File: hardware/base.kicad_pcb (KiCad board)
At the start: 4 copper layers, 100 x 85 mm, 316 parts, among them J101 USB-A, J102 TNG-Data-TOP, J103 TNG-Power-TOP, J301 MICROSDCARD, J302 Raspberry-Pi-Compute-Socket, J303 MICRO_HDMI, J304 USB Micro, J401 RJSLG-001TA1, P101 Debug, P102 Boot, P103 PE, P104 TST_GND, P105 TST_3V3P, P201 DI IN, P202 PWR IN, P203 TST_5V, P204 TST_GND, P301 TST_XMC_10, P302 TST_SCL, P303 TST_SDA, P304 TST_WP, P305 TST_3V3, P306 TST_1V8, P307 TST_XMC_11, P401 TST_1V2, Q301 2N7002P, Q302 2N7002P, Q303 2N7002P, Q304 2N7002P, Q305 2N7002P, T201 744272251, U101 USB2517, U102 MIC2026-1YM, U103 82400152, U104 XMC1302, U105 TPD4S010DQA, U106 TPD4S010DQA, U107 TPD4S010DQA, U108 AP7333-33SAG-7, U109 TPS22975, U110 TPS22975, U111 PCT2075DP, U112 VN7140AS, U201 ISO1211, U202 FPF2700MX, U203 BD90640HFP, U204 PAC1933, U301 PAM2306AYPAA, U302 PCF8523T, U303 FSUSB42MUX, U304 TPD4S010DQA, U305 TPD4S010DQA, U306 TPD4S010DQA, U307 82400152, U308 M24256-DFMN6TP, U309 AP2331, U310 SLB9670, U401 LAN7500, U402 93AA66, U403 TPD4S010DQA, U404 TPD4S010DQA, U405 PAM2306AYPAA, X101 24MHz, X301 32.768kHz, X401 25MHz_18pF

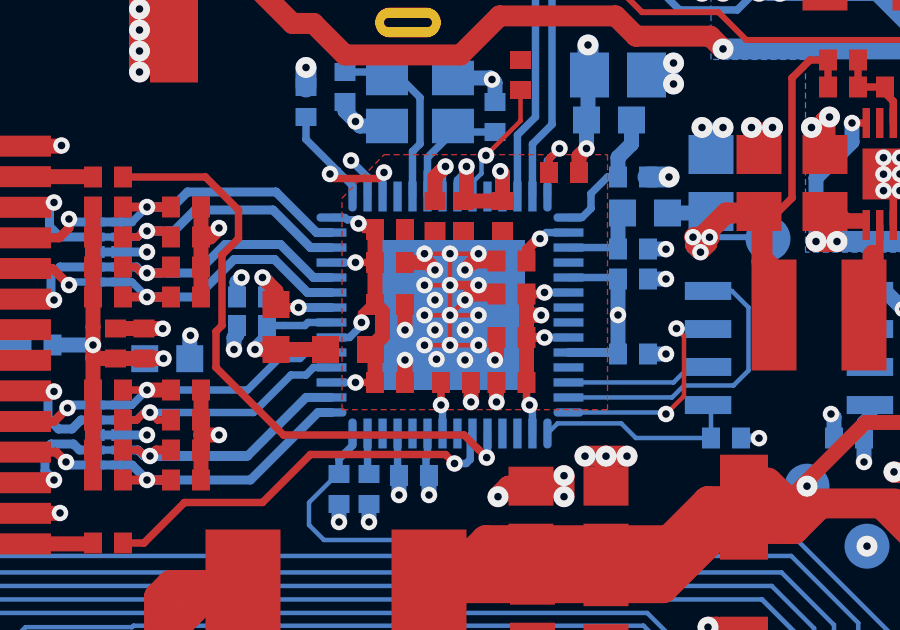
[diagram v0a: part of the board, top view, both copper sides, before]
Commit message: change ethernet capacitors to 33pF
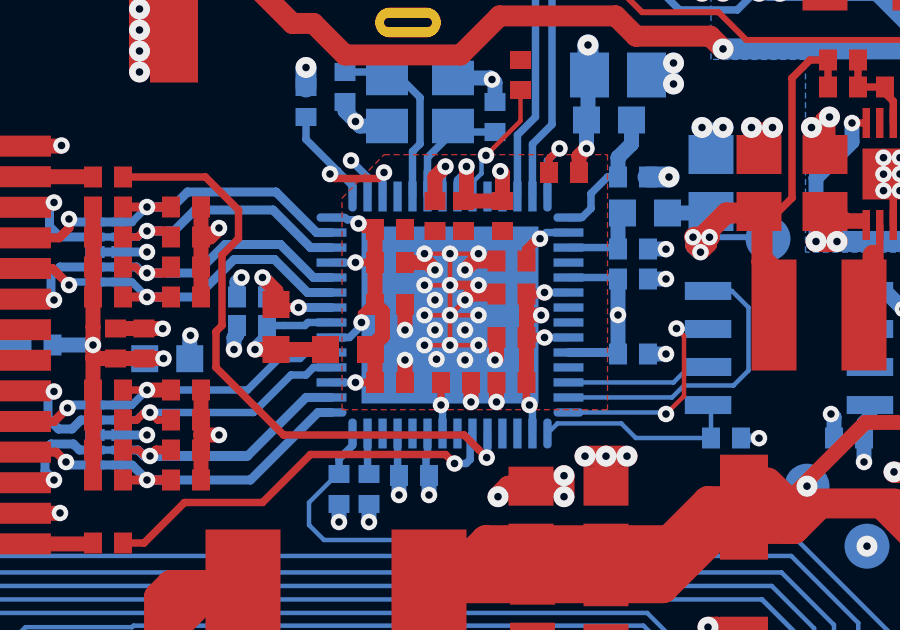
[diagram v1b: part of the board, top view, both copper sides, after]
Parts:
- C101, C102, C103, C104, C105, C106, C107, C110, C111, C112, C113, C114, C115, C116, C118, C119, C121, C122, C123, C124, C125, C126, C127, C128, C129, C130, C131, C132, C133, C134, C214, C221, C222, C227, C305, C306, C315, C316, C318, C319, C321, C322, C323, C324, C325, C327, C402, C403, C404, C405, C406, C407, C408, C409, C411, C412, C413, C414, C415, C416, C417, C418, C419, C420, C423, C424, C425, C426, C427, C428, C429, C430, C431, C432, C433, C436: footprint kicad-libraries:C0402F -> C0402F
- C108, C109, C117: footprint kicad-libraries:ELKO_63 -> ELKO_63
- C120, C210, C217, C320, C434: footprint kicad-libraries:C0603F -> C0603F
- C201, C202, C203, C204, C206, C207, C209, C211, C215, C226, C312, C313, C314: footprint kicad-libraries:C1206 -> C1206
- C302, R101, R102, R103, R104, R105, R106, R107, R108, R109, R110, R111, R112, R113, R114, R115, R116, R117, R210, R213, R216, R217, R218, R222, R301, R302, R303, R304, R305, R306, R307, R309, R313, R315, R316, R317, R318, R319, R320, R401, R402, R403, R404, R405, R406, R407, R408, R409, R410, R411, R412, R413, R414, R415, R416, R417, R418, R419, R420: footprint kicad-libraries:R0402F -> R0402F
- C317: footprint kicad-libraries:DSK -> DSK
- C421, C422: value 30pF -> 33pF; footprint kicad-libraries:C0402F -> C0402F
- D101, D207, D210: footprint kicad-libraries:LED-LP -> LED-LP
- D205, D206: footprint kicad-libraries:SOD-128 -> SOD-128
- D208, D301: footprint kicad-libraries:D0603F -> D0603F
- J102, J103: footprint kicad-libraries:TNG-40-TOP -> TNG-40-TOP
- J304: footprint kicad-libraries:USB-Micro-Vertical -> USB-Micro-Vertical
- L101, L401, L402, L403, L404, L405, R208, R212, R214, R215, R314: footprint kicad-libraries:R0603F -> R0603F
- L102, L103, L104, L105, L106, L107: footprint kicad-libraries:WE-CNSW-0603 -> WE-CNSW-0603
- L202: footprint kicad-libraries:WE-LHMI -> WE-LHMI
- L203: footprint kicad-libraries:SRP7030 -> SRP7030
- LED101: footprint kicad-libraries:LED-RGB-LP -> LED-RGB-LP
- P101: footprint kicad-libraries:DEBUG_PAD -> DEBUG_PAD
- P201, P202: footprint kicad-libraries:OQ_4P -> OQ_4P
- Q301, Q302, Q303, Q304, Q305: footprint kicad-libraries:SOT23GDS -> SOT23GDS
- R204, R206, R207, R209, R219, R220, R221: footprint kicad-libraries:R1206 -> R1206
- T201: footprint kicad-libraries:WE-SL5 -> WE-SL5
- U103, U307: footprint kicad-libraries:SOT563-SPEC -> SOT563-SPEC
- U105, U106, U107, U304, U305, U306, U403, U404: footprint kicad-libraries:TPD4S010DQA -> TPD4S010DQA
- U109, U110: footprint kicad-libraries:WSON8-2x2 -> WSON8-2x2
- U203: footprint kicad-libraries:BD906XX-C-HRP7 -> BD906XX-C-HRP7
- U301, U405: footprint kicad-libraries:WDFN12-3x3-0.45 -> WDFN12-3x3-0.45
- U309: footprint kicad-libraries:SOT23-3 -> SOT23-3
- U401: footprint kicad-libraries:QFN56-8x8mm-0.5mm -> QFN56-8x8mm-0.5mm
- U402: footprint kicad-libraries:SOIC8 -> SOIC8
- X101, X401: footprint kicad-libraries:CRYSTAL_3225 -> CRYSTAL_3225

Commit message: change slb capacitor
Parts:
- C320: value 1uF -> 2.2uF

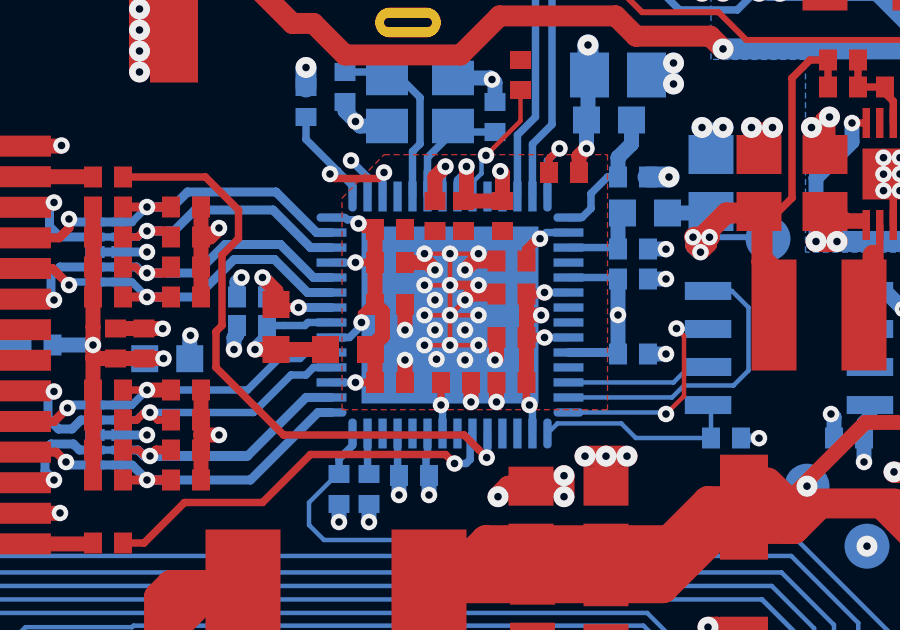
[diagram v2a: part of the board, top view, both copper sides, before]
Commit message: fix footprint
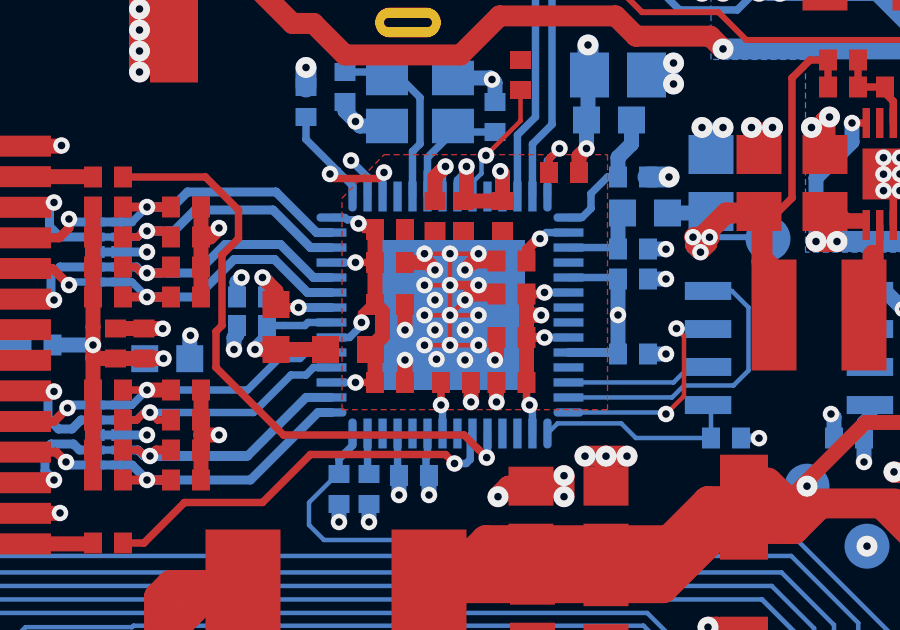
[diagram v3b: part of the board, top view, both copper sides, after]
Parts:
- C302: footprint R0402F -> kicad-libraries:C0402F

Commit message: fix 3d stuff
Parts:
- C101, C102, C103, C104, C105, C106, C107, C110, C111, C112, C113, C114, C115, C116, C118, C119, C121, C122, C123, C124, C125, C126, C127, C128, C129, C130, C131, C132, C133, C134, C214, C221, C222, C227, C305, C306, C315, C316, C318, C319, C321, C322, C323, C324, C325, C327, C402, C403, C404, C405, C406, C407, C408, C409, C411, C412, C413, C414, C415, C416, C417, C418, C419, C420, C421, C422, C423, C424, C425, C426, C427, C428, C429, C430, C431, C432, C433, C436: footprint C0402F -> kicad-libraries:C0402F
- C108, C109, C117: footprint ELKO_63 -> kicad-libraries:ELKO_63
- C120, C210, C217, C320, C434: footprint C0603F -> kicad-libraries:C0603F
- C201, C202, C203, C204, C206, C207, C209, C211, C215, C226, C312, C313, C314: footprint C1206 -> kicad-libraries:C1206
- C317: footprint DSK -> kicad-libraries:DSK
- D101, D207, D210: footprint LED-LP -> kicad-libraries:LED-LP
- D205, D206: footprint SOD-128 -> kicad-libraries:SOD-128
- D208, D301: footprint D0603F -> kicad-libraries:D0603F
- J102, J103: footprint TNG-40-TOP -> kicad-libraries:TNG-40-TOP
- J304: footprint USB-Micro-Vertical -> kicad-libraries:USB-Micro-Vertical
- L101, L401, L402, L403, L404, L405, R208, R212, R214, R215, R314: footprint R0603F -> kicad-libraries:R0603F
- L102, L103, L104, L105, L106, L107: footprint WE-CNSW-0603 -> kicad-libraries:WE-CNSW-0603
- L202: footprint WE-LHMI -> kicad-libraries:WE-LHMI
- L203: footprint SRP7030 -> kicad-libraries:SRP7030
- LED101: footprint LED-RGB-LP -> kicad-libraries:LED-RGB-LP
- P101: footprint DEBUG_PAD -> kicad-libraries:DEBUG_PAD
- P201, P202: footprint OQ_4P -> kicad-libraries:OQ_4P
- Q301, Q302, Q303, Q304, Q305: footprint SOT23GDS -> kicad-libraries:SOT23GDS
- R101, R102, R103, R104, R105, R106, R107, R108, R109, R110, R111, R112, R113, R114, R115, R116, R117, R210, R213, R216, R217, R218, R222, R301, R302, R303, R304, R305, R306, R307, R309, R313, R315, R316, R317, R318, R319, R320, R401, R402, R403, R404, R405, R406, R407, R408, R409, R410, R411, R412, R413, R414, R415, R416, R417, R418, R419, R420: footprint R0402F -> kicad-libraries:R0402F
- R204, R206, R207, R209, R219, R220, R221: footprint R1206 -> kicad-libraries:R1206
- T201: footprint WE-SL5 -> kicad-libraries:WE-SL5
- U103, U307: footprint SOT563-SPEC -> kicad-libraries:SOT563-SPEC
- U105, U106, U107, U304, U305, U306, U403, U404: footprint TPD4S010DQA -> kicad-libraries:TPD4S010DQA
- U109, U110: footprint WSON8-2x2 -> kicad-libraries:WSON8-2x2
- U203: footprint BD906XX-C-HRP7 -> kicad-libraries:BD906XX-C-HRP7
- U301, U405: footprint WDFN12-3x3-0.45 -> kicad-libraries:WDFN12-3x3-0.45
- U309: footprint SOT23-3 -> kicad-libraries:SOT23-3
- U401: footprint QFN56-8x8mm-0.5mm -> kicad-libraries:QFN56-8x8mm-0.5mm
- U402: footprint SOIC8 -> kicad-libraries:SOIC8
- X101, X401: footprint CRYSTAL_3225 -> kicad-libraries:CRYSTAL_3225

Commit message: add hint
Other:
- board text added: "Todo: RTC Power Supply Fix!"
